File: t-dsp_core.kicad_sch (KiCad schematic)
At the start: 268 parts, among them IC1 Logic Level Shifter - 74HCT2G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, J1 jumper, J10 JST-XH Connector, J11 JST-XH Connector, J12 RGB LED HEADEER, J13 Conn_01x02, J14 Conn_01x03, J15 Conn_01x01, J16 Conn_01x02, J17 Conn_02x04_Odd_Even, J18 Conn_02x02_Odd_Even, J19 Conn_01x01, J2 GROUND HEADER, J20 Conn_01x01, J21 jumper, J22 35RAPC4BV4, J23 35RAPC4BV4, J24 Conn_01x04, J25 PRT-14417, J26 73725-0110BLF, J27 GROUND HEADER, J3 jumper, J3V108 jumper, J4 jumper, J5 jumper, J6 jumper, J7 jumper, J8 PJRAS2X1S01X, J9 PJRAS2X1S01X, Q1 DMG2307L-7, Q2 DMG2307L-7, SW1 SW_SPST, SW10 SW_SPST, SW2 TL1105WF160Q - 3.15mm actuator, SW3 SW_SPST, SW4 SW_SPST, SW5 RotaryEncoder_Switch_MP, SW6 TL1105WF160Q - 3.15mm actuator, SW7 TL1105WF160Q - 3.15mm actuator, SW8 TL1105WF160Q - 3.15mm actuator, SW9 SW_SPST, T108 Tab, T109 Tab, T110 Tab, T111 Tab, U1 Teensy 4.1 - DEVKIT, U10 TPD4E02B04DQA, U109 3.3v LDO - LP5907-3.3, U11 Dual Buffer - SN74LVC2G125DCTR, U110 ESP32-S3-WROOM-1, U13 LT3045EMSE#TRPBF, U2 ESP32-DevKitC - DEVKIT, U3 Power Mux & Protect - TPS2116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, U4 Optoisolators - H11L1SM - 6-S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, U5 Dual Buffer - SN74LVC2G125DCTR, U6 Dual Buffer - SN74LVC2G125DCTR, U7 Dual Buffer - SN74LVC2G125DCTR, U8 Dual Buffer - SN74LVC2G125DCTR, U9 Dual Buffer - 74HCT2G17GW,125, Y1 audio clock

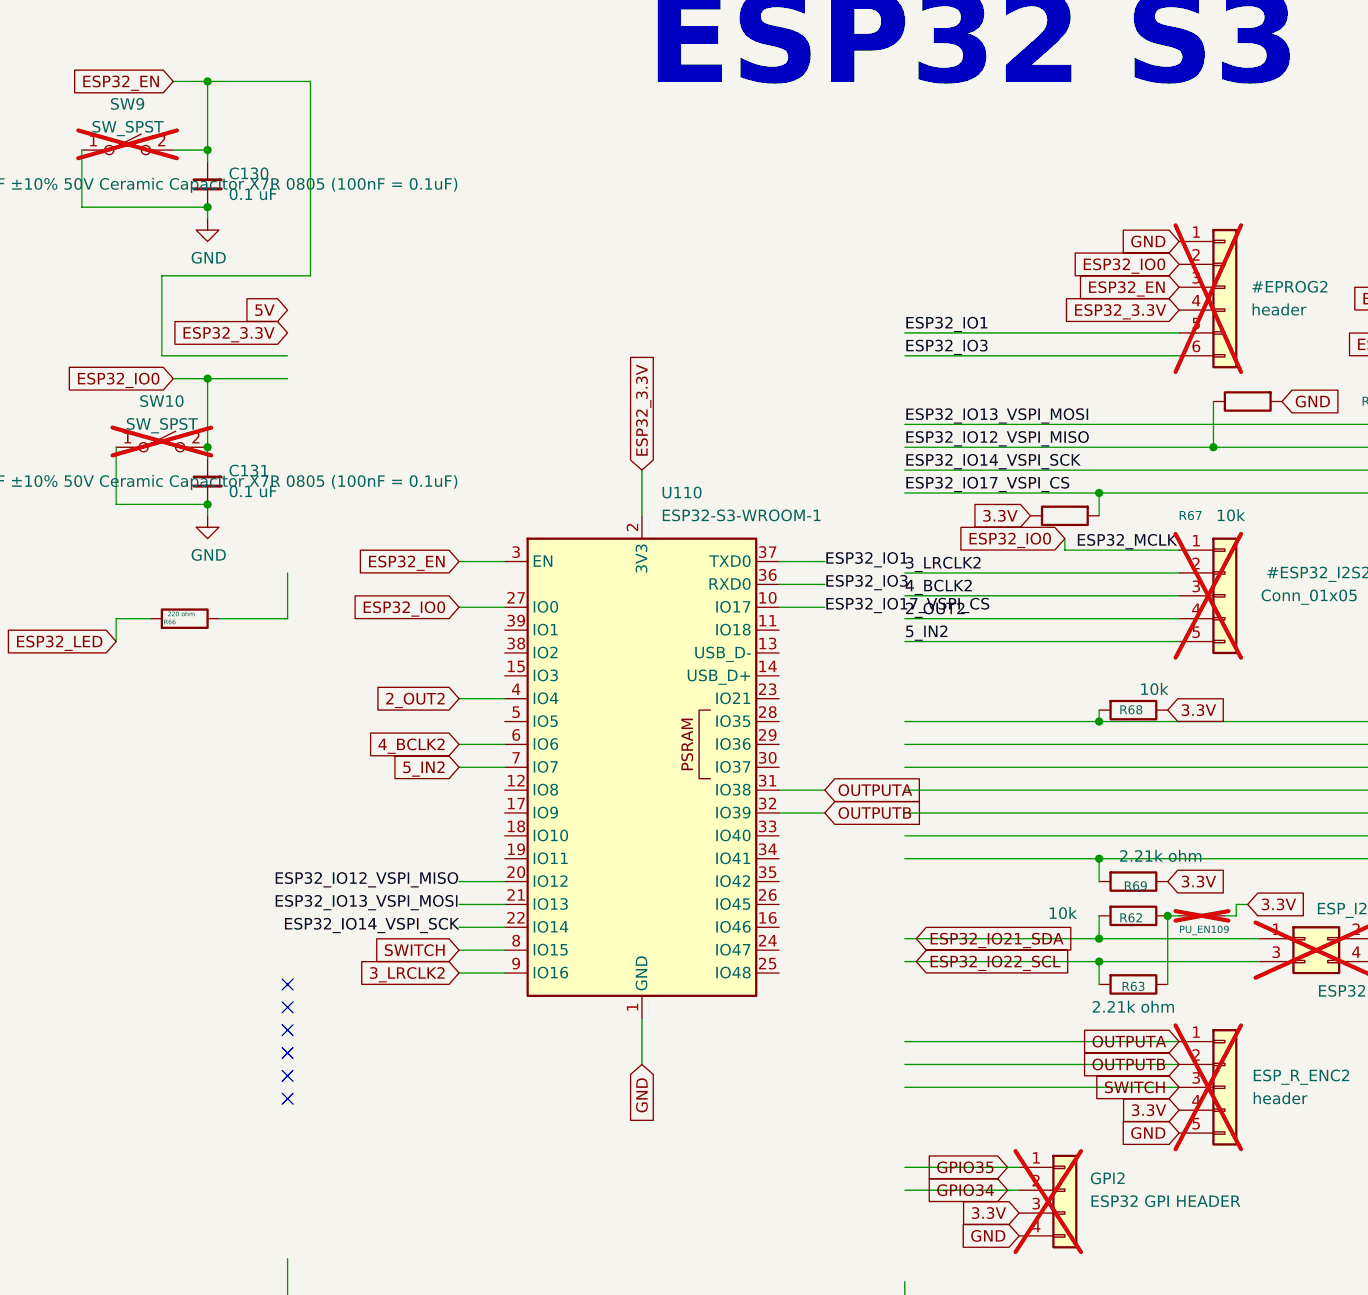
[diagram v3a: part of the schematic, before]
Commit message: Fix schematic made unloadable by Konnect, and revert ineffective renames
connect_to_net rewrites the entire schematic rather than patching it. That
rewrite dropped the arguments from the User paper size, leaving

  (paper "User")

which KiCad refuses to load: "need a number for 'width', line 6". Restored
to (paper "User" 1270 1270), the value held since c8ea8df. Verified by
kicad-cli sch export netlist, which now parses the file and emits a
532KB netlist.

The same rewrite also regenerated every Reference property from the
symbol instances blocks, which reverted the reference designator renames
made in db33470. Those renames were never effective in the first place:
edit_schematic_component writes only the Reference property and leaves
the instances block untouched, and KiCad netlists from instances. So
db33470 left the file internally inconsistent (property U110, instances
U13) rather than renamed. The current state is at least consistent.

Consequence: the seven collisions are live again and must be resolved in
eeschema, which updates both property and instances:

  C43 x2   C44 x2   R55 x2   R56 x2   R57 x2   R61 x2   U13 x2

The paste (241 elements) and the U110 wiring (17 stubs, 17 labels) are
both intact and unaffected.

Co-Authored-By: Claude Opus 5 <noreply@anthropic.com>
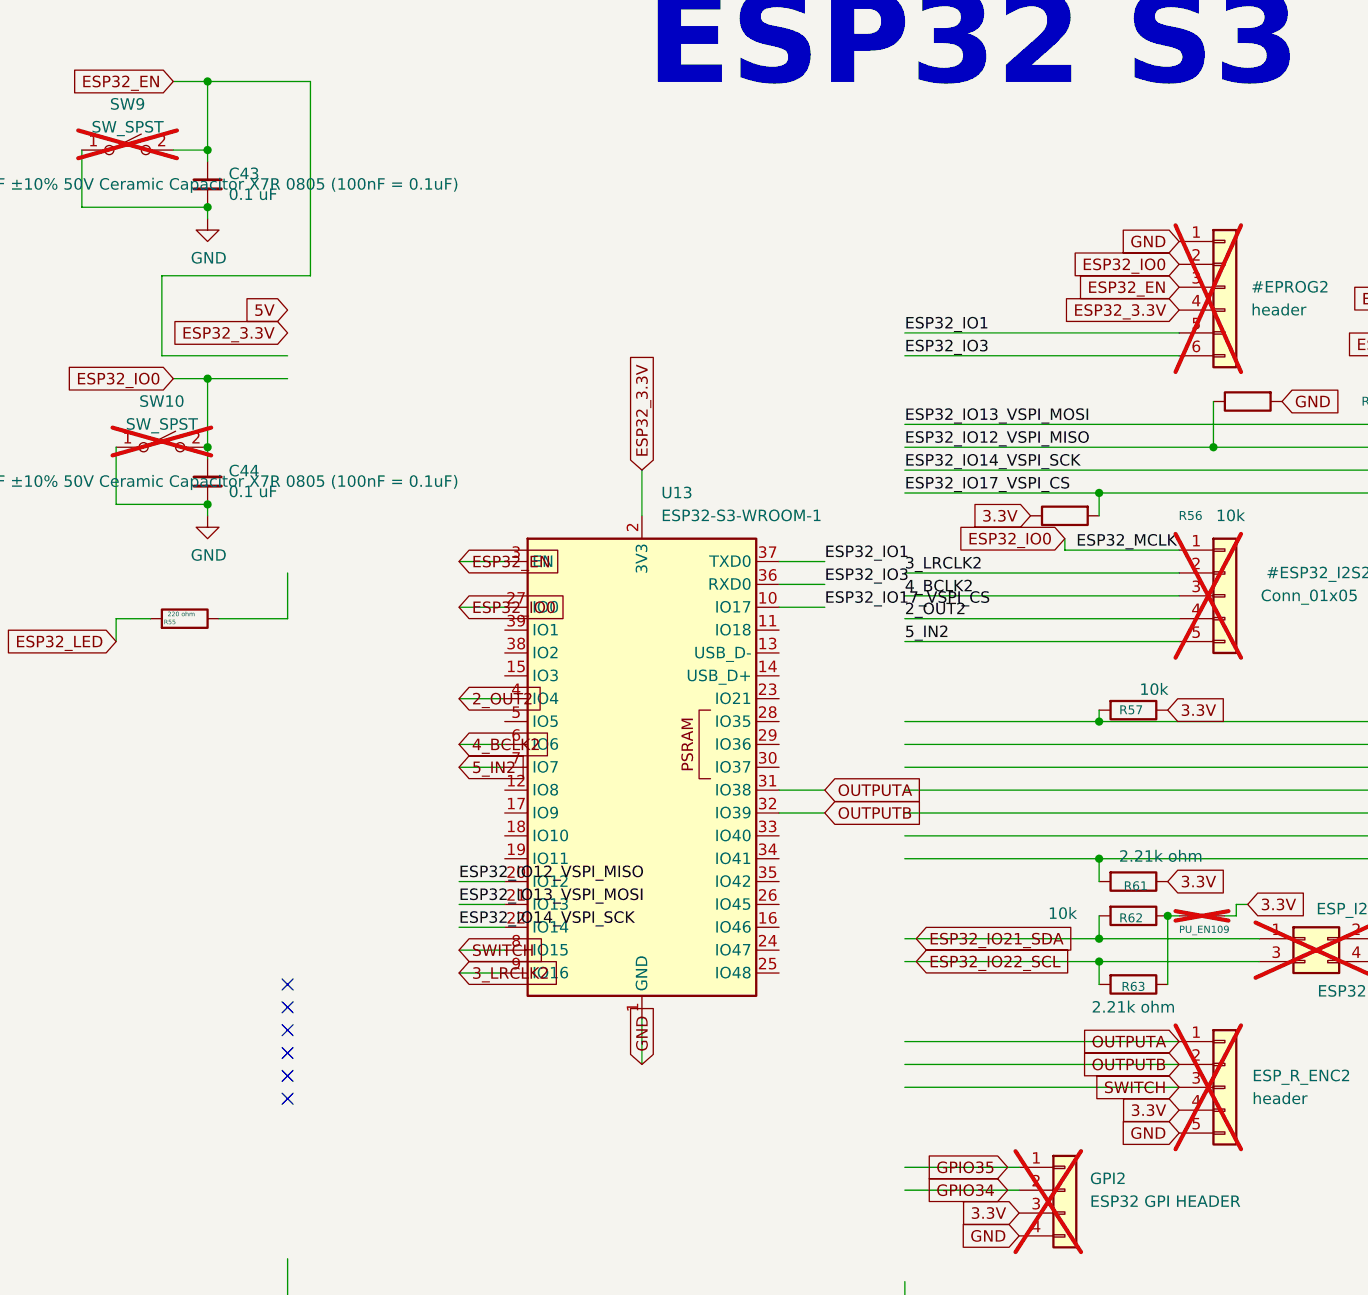
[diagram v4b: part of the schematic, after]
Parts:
- renumbered C130 to C43, C131 to C44, R66 to R55, R67 to R56, R68 to R57, R69 to R61, U110 to U13

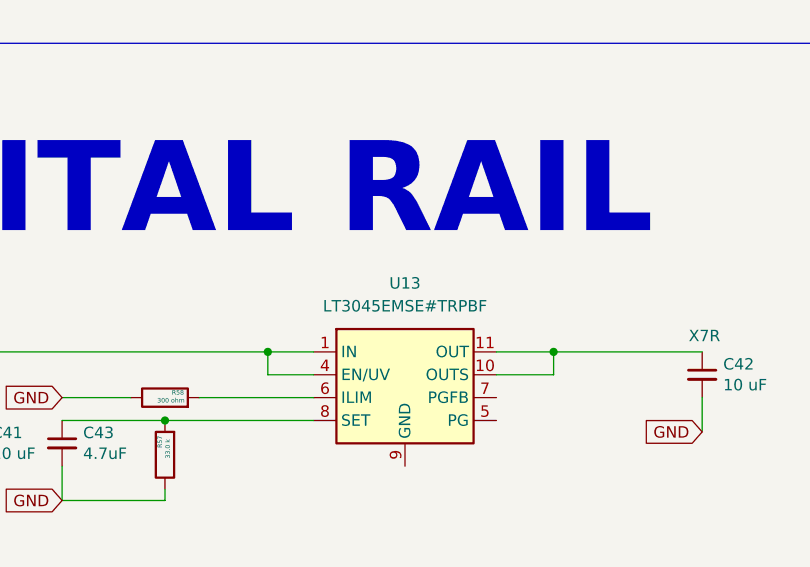
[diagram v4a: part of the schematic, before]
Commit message: Restore S3 section and resolve U13 collision (LT3045 -> U15)
Snapshot of manual work in eeschema before wiring the remaining 12 nets:
the ESP32-S3 box was restored with its 19 connections intact, U2 was
brought back, and the LT3045 regulator was renamed U15 so U13 belongs
solely to the ESP32-S3.

Six reference designators still collide (C43, C44, R55, R56, R57, R61).

Co-Authored-By: Claude Opus 5 <noreply@anthropic.com>
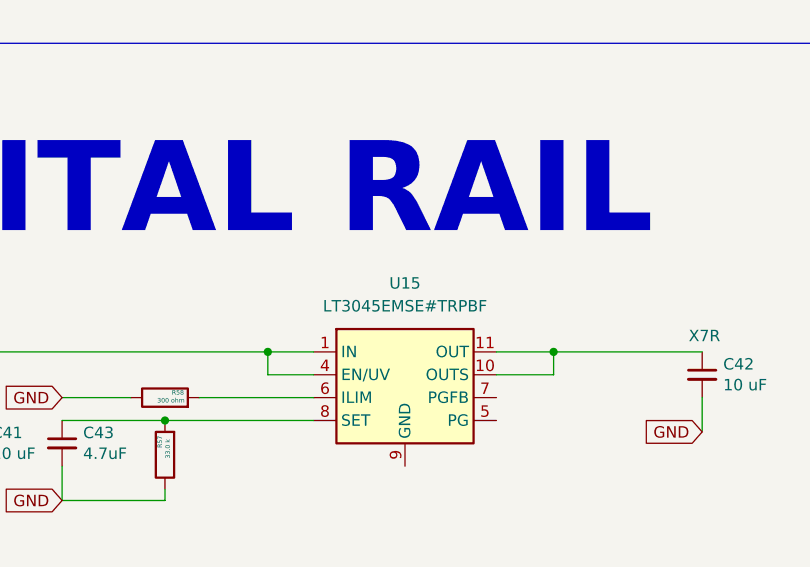
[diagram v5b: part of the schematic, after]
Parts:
- renumbered U13 to U15
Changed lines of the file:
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@@
 		(dnp no)
 		(fields_autoplaced yes)
-		(property "Reference" "U13"
+		(property "Reference" "U15"
 			(at 673.1 994.41 0)
 			(show_name no)
@@
 			(project "t-dsp_core"
 				(path "/6a0ff39d-771d-410f-9e7c-006586d81d16"
-					(reference "U13")
+					(reference "U15")
 					(unit 1)
 				)
@@
 	)
 	(symbol
+		(lib_name "SPH0645LM4H_2")
 		(lib_id "lib_sch:SPH0645LM4H")
 		(at 237.49 662.94 0)

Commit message: Wire ESP32-S3 TFT, I2C and GPI interfaces (11 nets)
Completes the U2 -> U13 net migration except for two cases noted below.
The S3 now carries 28 of the 30 nets on the classic ESP32-DevKitC.

Display and touch (ILI9341 + XPT2046), grouped on physically adjacent
module pins for layout:
  SCK   GPIO18 -> IO18 (11)    SDO   GPIO19 -> IO10 (18)
  T_CS  GPIO32 -> IO8  (12)    CS    GPIO15 -> IO11 (19)
  SDI   GPIO23 -> IO9  (17)    DC    GPIO2  -> IO2  (38)
  RESET GPIO4  -> IO42 (35)

I2C header:
  ESP32_IO21_SDA GPIO21 -> IO21 (23)
  ESP32_IO22_SCL GPIO22 -> IO47 (24)

GPI header:
  GPIO34 -> IO40 (33)     GPIO35 -> IO41 (34)

Not wired:
- 5V (U2 pin 19): a bare module has no 5V input. Needs the LDO.
- Net-(U2-*GPIO5): auto-named net joining U2 pin 29 to R18. Needs a real
  net name before the S3 can join it.

connect_to_net stripped the User paper dimensions again; restored in the
same pass and confirmed by netlist export.

Co-Authored-By: Claude Opus 5 <noreply@anthropic.com>
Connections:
- net CS: now also U13.19 (IO11)
- net DC: now also U13.38 (IO2)
- net ESP32_IO21_SDA: now also U13.23 (IO21)
- net ESP32_IO22_SCL: now also U13.24 (IO47)
- net GPIO34: now also U13.33 (IO40)
- net GPIO35: now also U13.34 (IO41)
- net RESET: now also U13.35 (IO42)
- net SCK: now also U13.11 (IO18)
- net SDI: now also U13.17 (IO9)
- net SDO: now also U13.18 (IO10)
- net T_CS: now also U13.12 (IO8)

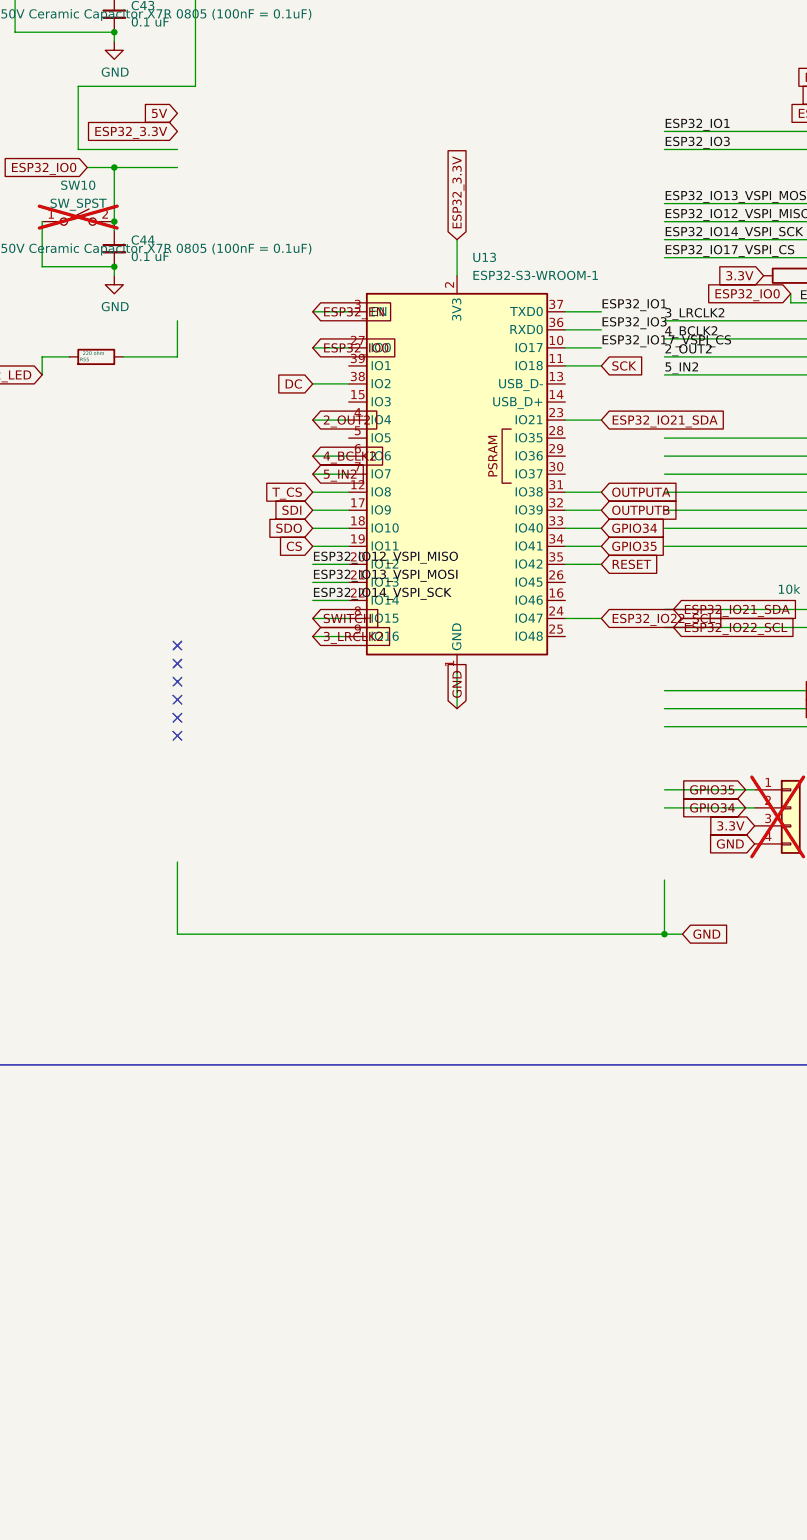
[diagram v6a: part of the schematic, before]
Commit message: Add 3.3V_DIG rail passives and move the ESP32-S3 onto it
Builds the digital 3.3V supply block for the ESP32-S3, minus the
regulator itself (see below).

Placed and wired:
  C130  10uF   5V input bulk
  C131  100nF  5V input HF
  C132  22uF   3.3V_DIG output bulk, sized for ESP32-S3 Wi-Fi transients
  C133  100nF  3.3V_DIG output HF
  R66   100k   EN pull-up to 5V, on net EN_3V3_DIG

U13 pin 2 (3V3) was repointed from ESP32_3.3V to the new 3.3V_DIG rail.
ESP32_3.3V now holds only U2 pin 1, and retires with the DevKitC.

Netlist confirms:
  3.3V_DIG    C132.1, C133.1, U13.2
  EN_3V3_DIG  R66.2
  ESP32_3.3V  U2.1

Also adds lib_sch/TLV76733DRVR.kicad_sym (1A 3.3V LDO with enable,
WSON-6) and registers it in sym-lib-table. register_symbol_library wrote
an absolute path; corrected to ${KIPRJMOD} so the repo stays portable.

The regulator U110 is NOT placed. Konnect's add_schematic_component
reports success but silently places nothing when the symbol is not
already embedded in the schematic's lib_symbols - it resolves symbols
through the same library reader that returns zero symbols for valid
.kicad_sym files. Only lib_ids already present in the file can be placed.
U110 has to be dropped in from eeschema.

Co-Authored-By: Claude Opus 5 <noreply@anthropic.com>
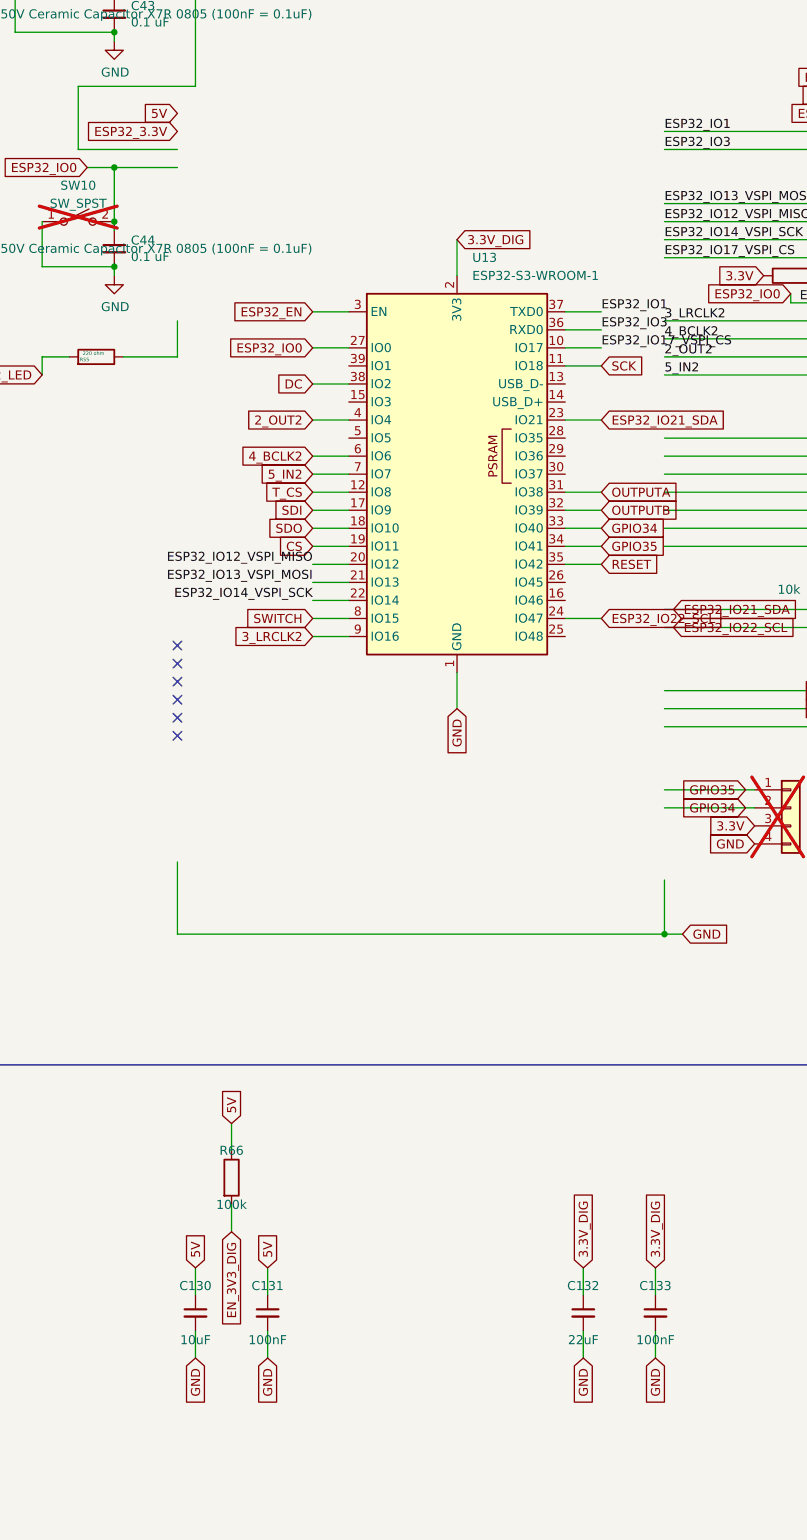
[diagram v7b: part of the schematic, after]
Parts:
- added C130: 10uF, symbol TEENSY_4.0_ESP32_AUDIO-rescue:C_Small-Device
- added C131, C133: 100nF, symbol TEENSY_4.0_ESP32_AUDIO-rescue:C_Small-Device
- added C132: 22uF, symbol TEENSY_4.0_ESP32_AUDIO-rescue:C_Small-Device
- added R66: 100k, symbol Device:R
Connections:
- net 5V: now also C130.1, C131.1, R66.1
- net ESP32_3.3V: no longer U13.2 (3V3)
- net GND: now also C130.2, C131.2, C132.2, C133.2
- new net 3.3V_DIG: C132.1, C133.1, U13.2 (3V3)
- new net EN_3V3_DIG: R66.2
